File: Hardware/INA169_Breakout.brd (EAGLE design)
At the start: 25.4 x 25.4 mm, 21 parts, among them U1 INA169

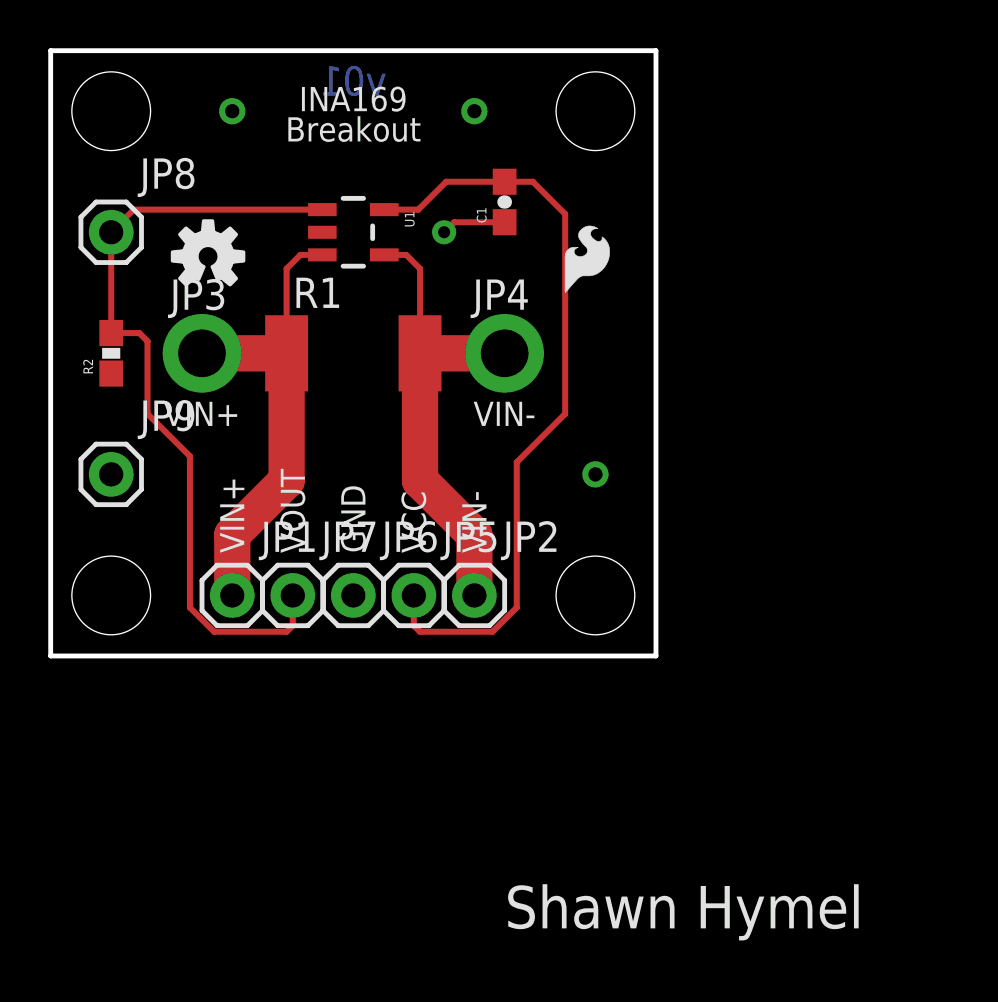
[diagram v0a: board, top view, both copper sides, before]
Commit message: Fixed changes from board review. Ready for prototype.
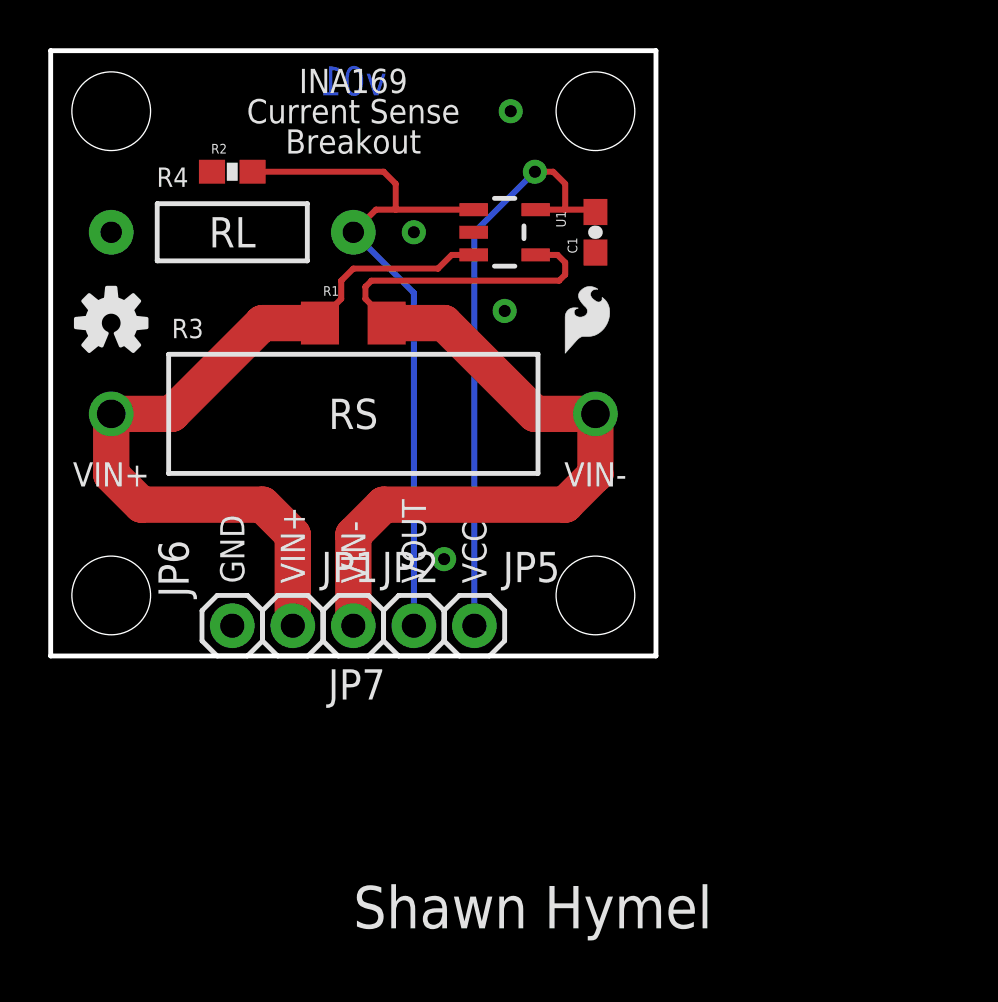
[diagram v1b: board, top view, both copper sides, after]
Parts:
- removed JP3, JP4: M01PTH_2MM, SparkFun-Connectors:1X01_2MM
- removed JP8, JP9: M01PTH, SparkFun-Connectors:1X01
- added R3: (no value), SparkFun-Resistors:AXIAL-0.8
- added R4: (no value), SparkFun-Resistors:AXIAL-0.4
- R1: value 0.1 -> 10; device SparkFun-Passives:R2512 -> SparkFun-Resistors:1206
- R2: value 10k\ -> 10k; device SparkFun-Passives:0603-RES -> SparkFun-Resistors:0603-RES
- moved FRAME1 11.4 mm to (-19.1, -11.4)
- moved LOGO1 9.40 mm to (21.1, 6.35)
- moved R2 9.16 mm to (7.62, 20.3), turned to 0 degrees
- moved U1 6.35 mm to (19.1, 17.8)
- moved JP2 5.24 mm to (12.7, 1.27)
- moved JP7 5.24 mm to (15.2, 1.27), turned to 180 degrees
- moved JP6 5.24 mm to (7.62, 1.27), turned to 90 degrees
- moved LOGO2 4.93 mm to (2.54, 14.0)
- moved C1 4.02 mm to (22.9, 17.8)
- moved JP5 2.84 mm to (17.8, 1.27)
- moved JP1 2.84 mm to (10.2, 1.27)
- moved LOGO3 2.54 mm to (21.6, 12.7)
- moved R1 1.27 mm to (12.7, 14.0)
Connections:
- net GND: now also R4.P$1; no longer JP9.1
- net VIN+: now also R3.P$1; no longer JP3.1
- net VIN-: now also R3.P$2; no longer JP4.1
- net VOUT: now also R4.P$2; no longer JP8.1
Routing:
- net VIN-: track 19.9 -> 40.3 mm
- net VIN+: track 19.9 -> 33.5 mm
- net VCC: track 32.1 -> 25.2 mm, vias 0 -> 1
- net VOUT: track 33.2 -> 30.3 mm
- net GND: track 2.71 -> 0.00 mm, vias 1 -> 4
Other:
- board text added: "0.5mA-50mA"
- board text added: "Current Sense"
- board text added: "RL"
- board text added: "RS"
- board text added: "Switch RS"
- board text added: "current range"
- board text added: "to change"

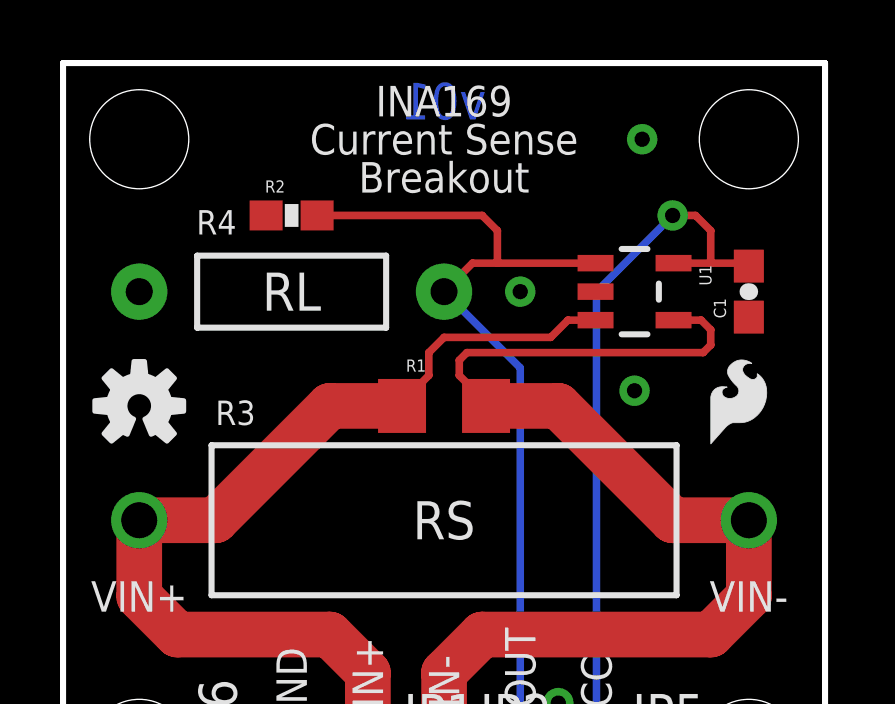
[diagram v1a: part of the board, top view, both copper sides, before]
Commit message: Fixed silkscreen. Ready for review.
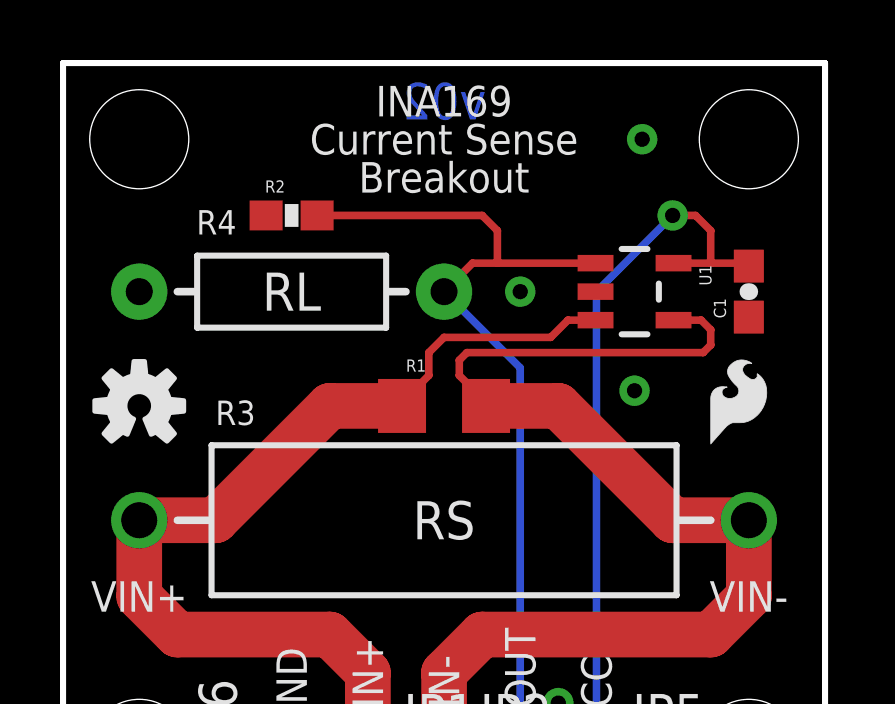
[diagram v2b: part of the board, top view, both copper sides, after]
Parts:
- moved LOGO1 1.27 mm to (22.4, 6.35)
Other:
- board text added: "5mA-50mA"
- board text added: "Replace RS"
- board text added: "v02"
- board text removed: "0.5mA-50mA"
- board text removed: "Switch RS"
- board text removed: "v01"
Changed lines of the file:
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@@
 <setting verticaltext="up"/>
 </settings>
-<grid distance="0.01" unitdist="inch" unit="inch" style="dots" multiple="1" display="yes" altdistance="0.005" altunitdist="inch" altunit="inch"/>
+<grid distance="0.05" unitdist="inch" unit="inch" style="dots" multiple="1" display="yes" altdistance="0.005" altunitdist="inch" altunit="inch"/>
 <layers>
 <layer number="1" name="Top" color="4" fill="1" visible="yes" active="yes"/>
-<layer number="16" name="Bottom" color="1" fill="1" visible="no" active="yes"/>
+<layer number="16" name="Bottom" color="1" fill="1" visible="yes" active="yes"/>
 <layer number="17" name="Pads" color="2" fill="1" visible="yes" active="yes"/>
 <layer number="18" name="Vias" color="2" fill="1" visible="yes" active="yes"/>
@@
 <layer number="20" name="Dimension" color="6" fill="1" visible="yes" active="yes"/>
 <layer number="21" name="tPlace" color="16" fill="1" visible="yes" active="yes"/>
-<layer number="22" name="bPlace" color="14" fill="1" visible="no" active="yes"/>
+<layer number="22" name="bPlace" color="14" fill="1" visible="yes" active="yes"/>
 <layer number="23" name="tOrigins" color="15" fill="1" visible="yes" active="yes"/>
-<layer number="24" name="bOrigins" color="15" fill="1" visible="no" active="yes"/>
+<layer number="24" name="bOrigins" color="15" fill="1" visible="yes" active="yes"/>
 <layer number="25" name="tNames" color="7" fill="1" visible="no" active="yes"/>
 <layer number="26" name="bNames" color="7" fill="1" visible="no" active="yes"/>
@@
 <layer number="43" name="vRestrict" color="2" fill="10" visible="no" active="yes"/>
 <layer number="44" name="Drills" color="7" fill="1" visible="no" active="yes"/>
-<layer number="45" name="Holes" color="7" fill="1" visible="no" active="yes"/>
+<layer number="45" name="Holes" color="7" fill="1" visible="yes" active="yes"/>
 <layer number="46" name="Milling" color="3" fill="1" visible="no" active="yes"/>
-<layer number="51" name="tDocu" color="6" fill="1" visible="no" active="yes"/>
+<layer number="51" name="tDocu" color="6" fill="1" visible="yes" active="yes"/>
 <layer number="52" name="bDocu" color="7" fill="1" visible="no" active="yes"/>
 <layer number="33" name="tFinish" color="6" fill="3" visible="no" active="no"/>
@@
 <text x="12.7" y="24.13" size="1.016" layer="21" font="vector" ratio="19" align="center">INA169</text>
 <text x="12.7" y="21.59" size="1.016" layer="21" font="vector" ratio="19" align="center">Breakout</text>
-<text x="12.7" y="24.13" size="1.2192" layer="16" font="vector" ratio="15" rot="MR0" align="center">v01</text>
+<text x="12.7" y="24.13" size="1.2192" layer="16" font="vector" ratio="15" rot="MR0" align="center">v02</text>
 <text x="12.7" y="-11.43" size="1.778" layer="25">Shawn Hymel</text>
 <rectangle x1="18.542" y1="16.51" x2="19.558" y2="19.05" layer="41"/>
@@
 <text x="12.7" y="10.16" size="1.27" layer="21" font="vector" ratio="15" align="center">RS</text>
 <text x="7.62" y="17.78" size="1.27" layer="21" font="vector" ratio="15" align="center">RL</text>
-<text x="10.16" y="11.43" size="1.016" layer="22" font="vector" ratio="15" rot="MR90">0.5mA-50mA</text>
-<text x="7.62" y="11.43" size="1.016" layer="22" font="vector" ratio="15" rot="MR90">Switch RS</text>
+<text x="10.16" y="11.43" size="1.016" layer="22" font="vector" ratio="15" rot="MR90">5mA-50mA</text>
+<text x="7.62" y="11.43" size="1.016" layer="22" font="vector" ratio="15" rot="MR90">Replace RS</text>
 <text x="6.35" y="11.43" size="1.016" layer="22" font="vector" ratio="15" rot="MR90">to change</text>
 <text x="5.08" y="11.43" size="1.016" layer="22" font="vector" ratio="15" rot="MR90">current range</text>
@@
 <text x="12.7" y="3.048" size="1.016" layer="22" font="vector" ratio="19" rot="MR90" align="center-left">VIN-</text>
 <rectangle x1="19.304" y1="17.272" x2="22.098" y2="18.288" layer="41"/>
+<wire x1="3.81" y1="10.16" x2="4.9022" y2="10.16" width="0.254" layer="21"/>
+<wire x1="21.59" y1="10.16" x2="20.4978" y2="10.16" width="0.254" layer="21"/>
+<wire x1="3.81" y1="17.78" x2="4.4196" y2="17.78" width="0.254" layer="21"/>
+<wire x1="11.43" y1="17.78" x2="10.8204" y2="17.78" width="0.254" layer="21"/>
 </plain>
 <attributes>
@@
 <element name="STANDOFF3" library="SparkFun-Electromechanical" package="STAND-OFF" value="STAND-OFF" x="22.86" y="2.54"/>
 <element name="STANDOFF4" library="SparkFun-Electromechanical" package="STAND-OFF" value="STAND-OFF" x="2.54" y="2.54"/>
-<element name="LOGO1" library="SparkFun-Aesthetics" package="SFE-NEW-WEBLOGO" value="LOGO-SFENEW" x="21.082" y="6.35" rot="MR0"/>
+<element name="LOGO1" library="SparkFun-Aesthetics" package="SFE-NEW-WEBLOGO" value="LOGO-SFENEW" x="22.352" y="6.35" rot="MR0"/>
 <element name="LOGO2" library="SparkFun-Aesthetics" package="OSHW-LOGO-S" value="OSHW-LOGOS" x="2.54" y="13.97"/>
 <element name="LOGO3" library="SparkFun-Aesthetics" package="SFE-LOGO-FLAME" value="LOGO-SFESK" x="21.59" y="12.7"/>

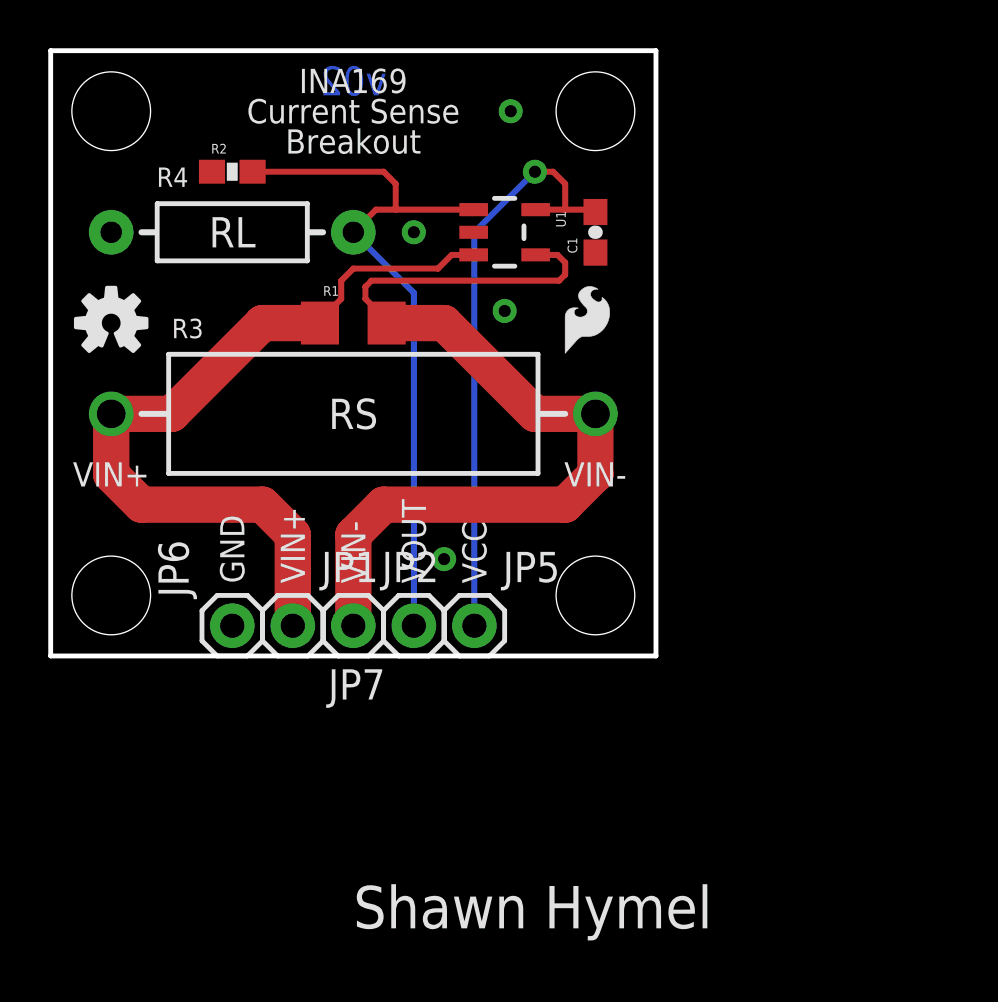
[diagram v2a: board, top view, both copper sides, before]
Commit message: Added tables on sch, added pads on brd
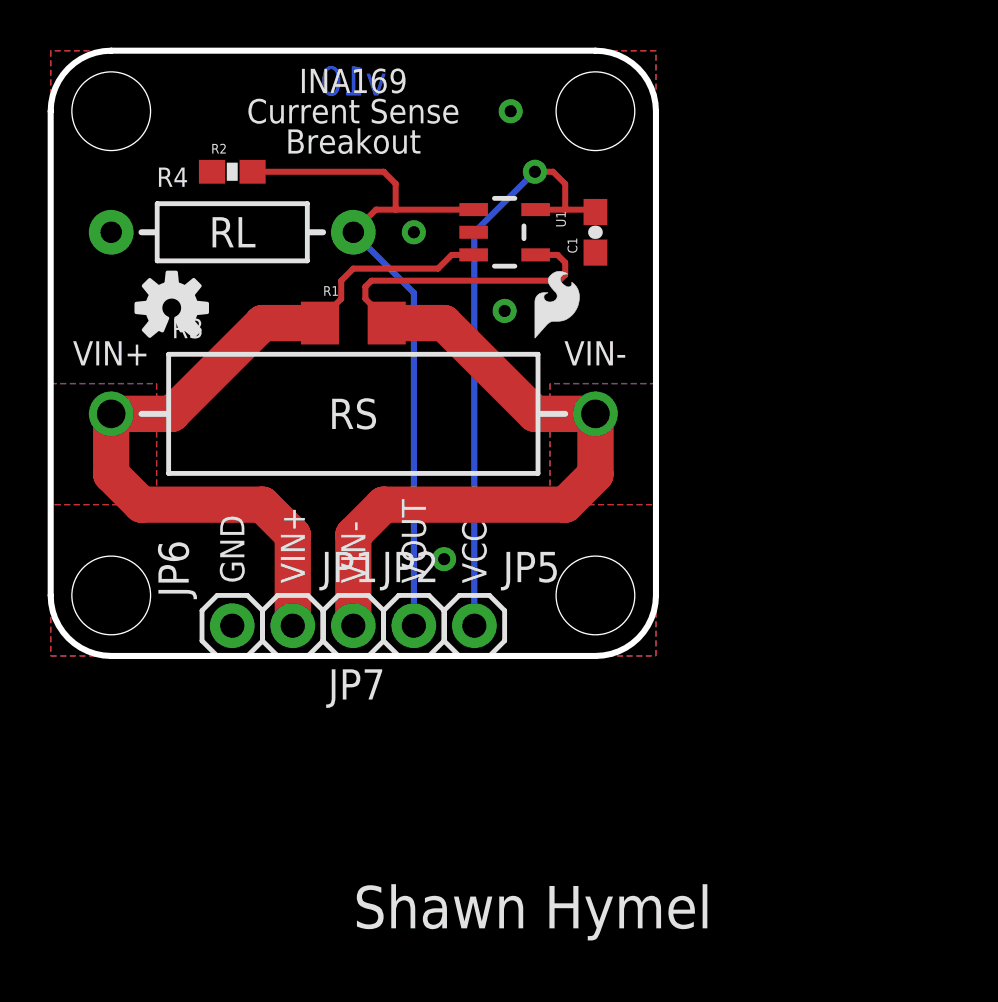
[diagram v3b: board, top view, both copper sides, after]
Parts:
- moved LOGO2 2.62 mm to (5.08, 14.6)
- moved LOGO3 1.42 mm to (20.3, 13.3)
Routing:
- added copper zone on layer 1, net VIN+
- added copper zone on layer 16, net VIN+
- added copper zone on layer 1, net VIN-
- added copper zone on layer 16, net VIN-
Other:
- outline, holes or cut-outs redrawn
- board text added: "3.5mA-35mA"
- board text added: "Knock Out"
- board text added: "v10"
- board text removed: "5mA-50mA"
- board text removed: "v02"

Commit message: Changed to smaller SFE logo on brd
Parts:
- LOGO1: value LOGO-SFENEW -> SFE_LOGO_NAME_FLAME.1_INCH; device SparkFun-Aesthetics:SFE-NEW-WEBLOGO -> SparkFun-Aesthetics:SFE_LOGO_NAME_FLAME_.1
- moved LOGO1 8.32 mm to (15.2, 10.7), turned to 90 degrees
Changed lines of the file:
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@@
 <setting verticaltext="up"/>
 </settings>
-<grid distance="0.05" unitdist="inch" unit="inch" style="dots" multiple="1" display="yes" altdistance="0.005" altunitdist="inch" altunit="inch"/>
+<grid distance="0.05" unitdist="inch" unit="inch" style="dots" multiple="1" display="yes" altdistance="0.025" altunitdist="inch" altunit="inch"/>
 <layers>
 <layer number="1" name="Top" color="4" fill="1" visible="yes" active="yes"/>
@@
 <element name="STANDOFF3" library="SparkFun-Electromechanical" package="STAND-OFF" value="STAND-OFF" x="22.86" y="2.54"/>
 <element name="STANDOFF4" library="SparkFun-Electromechanical" package="STAND-OFF" value="STAND-OFF" x="2.54" y="2.54"/>
-<element name="LOGO1" library="SparkFun-Aesthetics" package="SFE-NEW-WEBLOGO" value="LOGO-SFENEW" x="22.352" y="6.35" rot="MR0"/>
+<element name="LOGO1" library="SparkFun-Aesthetics" package="SFE_LOGO_NAME_FLAME_.1" value="SFE_LOGO_NAME_FLAME.1_INCH" x="15.24" y="10.668" rot="MR90"/>
 <element name="LOGO2" library="SparkFun-Aesthetics" package="OSHW-LOGO-S" value="OSHW-LOGOS" x="5.08" y="14.605"/>
 <element name="LOGO3" library="SparkFun-Aesthetics" package="SFE-LOGO-FLAME" value="LOGO-SFESK" x="20.32" y="13.335"/>
